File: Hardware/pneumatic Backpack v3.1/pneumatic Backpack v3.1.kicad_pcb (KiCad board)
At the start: 2 copper layers, 64 x 73 mm, 82 parts, among them J1 Conn_01x12_Pin, J10 Conn_01x02_Pin, J11 Conn_01x02_Pin, J2 Conn_01x01_Pin, J3 Conn_02x16_Top_Bottom, J4 Conn_02x16_Top_Bottom, J5 Conn_01x12_Pin, J9 Conn_01x02_Pin, U1 ESP32-S3-DEVKITC-1-N8R2, U3 INA332AIDGKR, U4 INA332AIDGKR, U5 MCZ33996EK

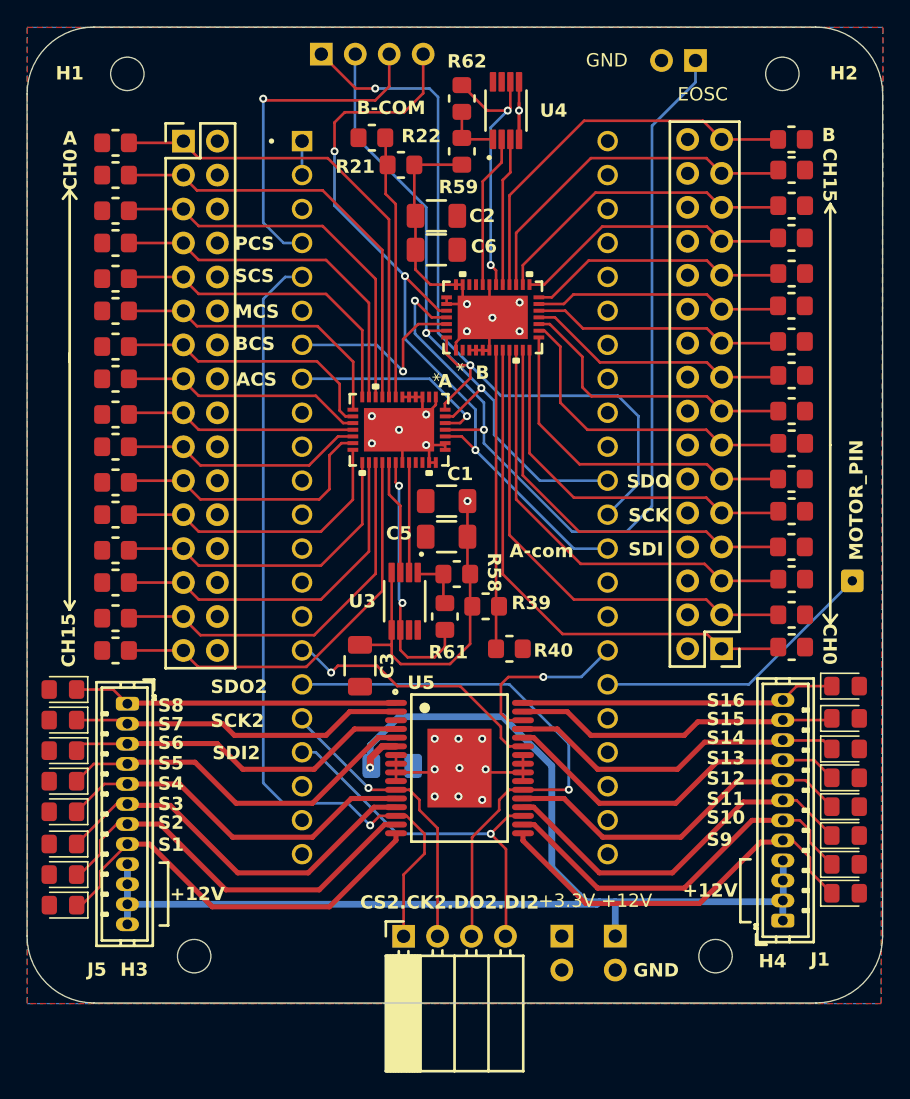
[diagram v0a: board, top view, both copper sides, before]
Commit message: added diods to the leds
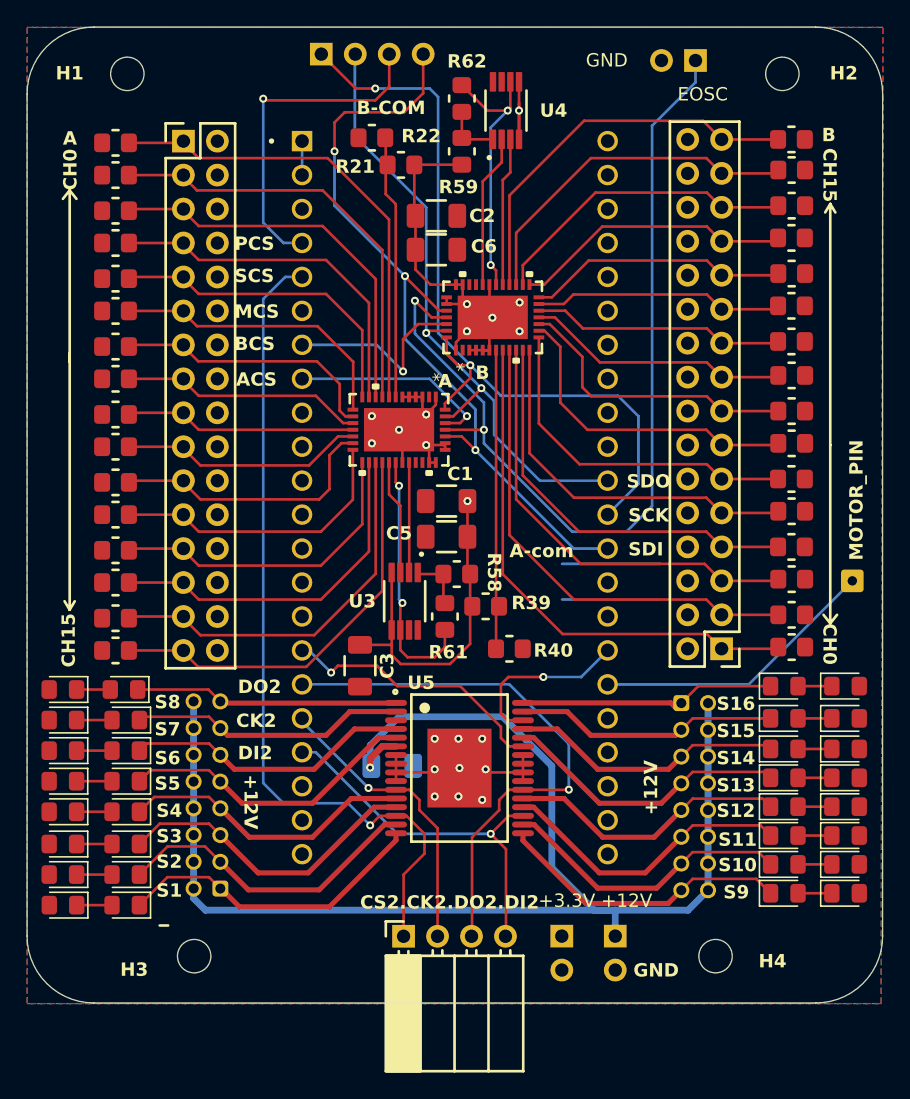
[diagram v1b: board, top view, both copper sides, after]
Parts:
- added D17: D, Diode_SMD:D_0805_2012Metric_Pad1.15x1.40mm_HandSolder, F.Cu at (103.3, 114.6)
- added D18: D, Diode_SMD:D_0805_2012Metric_Pad1.15x1.40mm_HandSolder, F.Cu at (103.4, 116.8)
- added D19: D, Diode_SMD:D_0805_2012Metric_Pad1.15x1.40mm_HandSolder, F.Cu at (103.4, 119.1)
- added D20: D, Diode_SMD:D_0805_2012Metric_Pad1.15x1.40mm_HandSolder, F.Cu at (103.4, 121.4)
- added D21: D, Diode_SMD:D_0805_2012Metric_Pad1.15x1.40mm_HandSolder, F.Cu at (103.4, 123.7)
- added D22: D, Diode_SMD:D_0805_2012Metric_Pad1.15x1.40mm_HandSolder, F.Cu at (103.4, 126.1)
- added D23: D, Diode_SMD:D_0805_2012Metric_Pad1.15x1.40mm_HandSolder, F.Cu at (103.4, 128.4)
- added D24: D, Diode_SMD:D_0805_2012Metric_Pad1.15x1.40mm_HandSolder, F.Cu at (103.4, 130.7)
- added D25: D, Diode_SMD:D_0805_2012Metric_Pad1.15x1.40mm_HandSolder, F.Cu at (152.6, 129.8)
- added D26: D, Diode_SMD:D_0805_2012Metric_Pad1.15x1.40mm_HandSolder, F.Cu at (152.6, 127.6)
- added D27: D, Diode_SMD:D_0805_2012Metric_Pad1.15x1.40mm_HandSolder, F.Cu at (152.6, 125.5)
- added D28: D, Diode_SMD:D_0805_2012Metric_Pad1.15x1.40mm_HandSolder, F.Cu at (152.6, 123.3)
- added D29: D, Diode_SMD:D_0805_2012Metric_Pad1.15x1.40mm_HandSolder, F.Cu at (152.6, 121.2)
- added D30: D, Diode_SMD:D_0805_2012Metric_Pad1.15x1.40mm_HandSolder, F.Cu at (152.6, 119.0)
- added D31: D, Diode_SMD:D_0805_2012Metric_Pad1.15x1.40mm_HandSolder, F.Cu at (152.6, 116.7)
- added D32: D, Diode_SMD:D_0805_2012Metric_Pad1.15x1.40mm_HandSolder, F.Cu at (152.6, 114.3)
- J1, J5: value Conn_01x12_Pin -> Conn_02x08_Odd_Even; footprint Connector_JST:JST_ZH_B12B-ZR_1x12_P1.50mm_Vertical -> Connector_JST:JST_PHD_S16B-PHDSS_2x08_P2.00mm_Horizontal; moved to B.Cu
- R21, R22, R23, R24, R25, R26, R27, R28, R29, R30, R31, R32, R33, R34, R35, R36, R37, R38, R39, R40, R41, R42, R43, R44, R45, R46, R47, R48, R49, R50, R51, R52, R53, R54, R55, R56: value 100 -> 100k
- moved J1 18.0 mm to (144.9, 115.6), turned to -90 degrees
- moved J5 15.5 mm to (110.5, 129.4), turned to 90 degrees
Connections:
- D1 pad 1: S8 -> Net-(D1-K)
- D10 pad 1: S15 -> Net-(D10-K)
- D11 pad 1: S14 -> Net-(D11-K)
- D12 pad 1: S13 -> Net-(D12-K)
- D13 pad 1: S12 -> Net-(D13-K)
- D14 pad 1: S11 -> Net-(D14-K)
- D15 pad 1: S10 -> Net-(D15-K)
- D16 pad 1: S9 -> Net-(D16-K)
- D2 pad 1: S7 -> Net-(D18-A)
- D3 pad 1: S6 -> Net-(D19-A)
- D4 pad 1: S5 -> Net-(D20-A)
- D5 pad 1: S4 -> Net-(D21-A)
- D6 pad 1: S3 -> Net-(D22-A)
- D7 pad 1: S2 -> Net-(D23-A)
- D8 pad 1: S1 -> Net-(D24-A)
- D9 pad 1: S16 -> Net-(D32-A)
- J1 pad 1: +12V -> S16
- J1 pad 10: S14 -> +12V
- J1 pad 11: S15 -> S11
- J1 pad 12: S16 -> +12V
- J1 pad 3: +12V -> S15
- J1 pad 5: S9 -> S14
- J1 pad 6: S10 -> +12V
- J1 pad 7: S11 -> S13
- J1 pad 8: S12 -> +12V
- J1 pad 9: S13 -> S12
- J5 pad 1: S8 -> S1
- J5 pad 11: +12V -> S6
- J5 pad 2: S7 -> +12V
- J5 pad 3: S6 -> S2
- J5 pad 4: S5 -> +12V
- J5 pad 5: S4 -> S3
- J5 pad 6: S3 -> +12V
- J5 pad 7: S2 -> S4
- J5 pad 8: S1 -> +12V
- J5 pad 9: +12V -> S5
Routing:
- net GND: track 84.5 -> 99.3 mm
- net +12V: track 96.1 -> 104.5 mm
- net S9: track 29.6 -> 21.7 mm
- net S10: track 29.1 -> 21.5 mm
- net S1: track 31.0 -> 23.6 mm
- net S2: track 30.1 -> 23.4 mm
- net S11: track 28.5 -> 21.8 mm
- net S12: track 26.9 -> 20.6 mm
- net S3: track 29.5 -> 23.4 mm
- net S13: track 27.0 -> 21.2 mm
- net S4: track 27.6 -> 22.1 mm
- net S14: track 25.5 -> 20.1 mm
- net S5: track 27.8 -> 22.6 mm
- net S15: track 24.4 -> 19.2 mm
- net S6: track 26.3 -> 21.5 mm
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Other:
- board text added: "CK2"
- board text added: "DI2"
- board text added: "DO2"
- board text removed: "SCK2"
- board text removed: "SDI2"
- board text removed: "SDO2"
